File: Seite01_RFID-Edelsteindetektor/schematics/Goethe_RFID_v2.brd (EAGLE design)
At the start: 57.1 x 53.3 mm, 61 parts, among them IC1 LM1086-ADJ, IC2 LM2937, M1 ARDUINO_R3_SMALL, Q1 IRF8313P, Q2 IRF8313P, Q3 IRF8313P, X1 12V supply

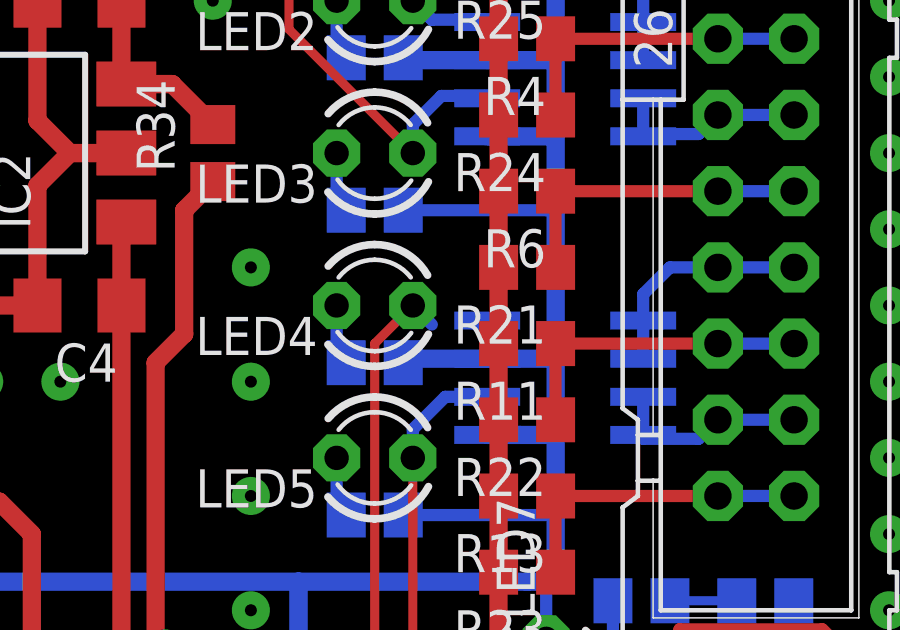
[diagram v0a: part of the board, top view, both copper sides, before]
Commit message: Fix missing wire on signal LED4
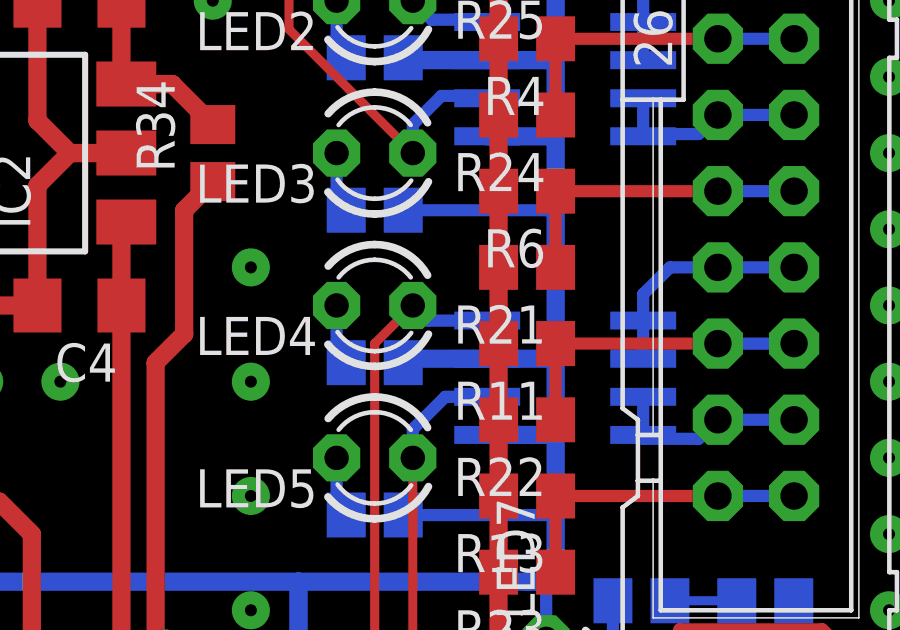
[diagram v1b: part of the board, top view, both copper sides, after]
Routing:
- net A0_LED4: track 22.8 -> 24.6 mm
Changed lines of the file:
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@@
 <grid distance="1" unitdist="mm" unit="mm" style="dots" multiple="1" display="yes" altdistance="0.00625" altunitdist="inch" altunit="mm"/>
 <layers>
-<layer number="1" name="Top" color="4" fill="1" visible="yes" active="yes"/>
+<layer number="1" name="Top" color="4" fill="1" visible="no" active="yes"/>
 <layer number="16" name="Bottom" color="1" fill="1" visible="yes" active="yes"/>
 <layer number="17" name="Pads" color="2" fill="1" visible="yes" active="yes"/>
 <layer number="18" name="Vias" color="2" fill="1" visible="yes" active="yes"/>
-<layer number="19" name="Unrouted" color="6" fill="1" visible="no" active="yes"/>
+<layer number="19" name="Unrouted" color="6" fill="1" visible="yes" active="yes"/>
 <layer number="20" name="Dimension" color="15" fill="1" visible="yes" active="yes"/>
 <layer number="21" name="tPlace" color="7" fill="1" visible="no" active="yes"/>
@@
 <contactref element="M1" pad="A0"/>
 <contactref element="LED4" pad="A"/>
-<wire x1="36.195" y1="18.415" x2="35.56" y2="19.05" width="0.4064" layer="16"/>
 <via x="33.02" y="6.0325" extent="1-16" drill="0.4" diameter="1.27" shape="octagon"/>
 <wire x1="33.02" y1="6.0325" x2="34.29" y2="7.3025" width="0.3048" layer="1"/>
@@
 <wire x1="34.6075" y1="4.445" x2="37.465" y2="4.445" width="0.3048" layer="16"/>
 <wire x1="37.465" y1="4.445" x2="39.37" y2="2.54" width="0.3048" layer="16"/>
-<wire x1="36.195" y1="18.415" x2="38.04" y2="18.545" width="0" layer="19" extent="16-16"/>
+<wire x1="35.56" y1="19.05" x2="36.065" y2="18.545" width="0.4064" layer="16"/>
+<wire x1="36.065" y1="18.545" x2="38.04" y2="18.545" width="0.4064" layer="16"/>
 </signal>
 <signal name="A1_LED5">
